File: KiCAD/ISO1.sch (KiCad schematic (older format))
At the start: 5 parts, among them J39 Conn_02x04_Odd_Even, J40 Conn_02x04_Odd_Even, U14 ISO7341c

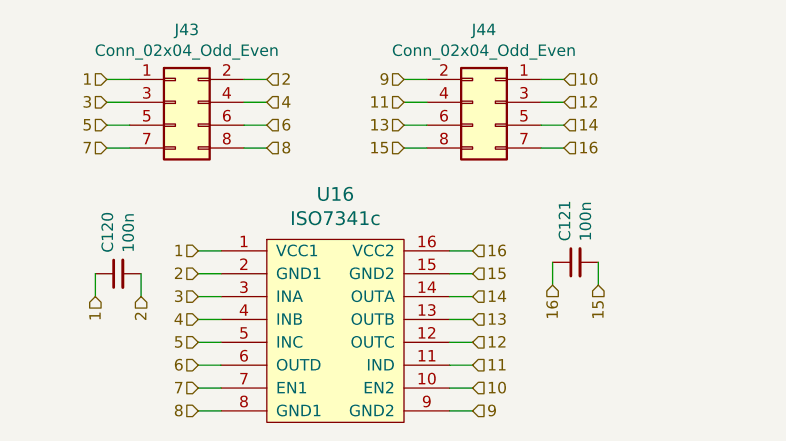
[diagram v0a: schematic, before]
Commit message: added usb, crystals
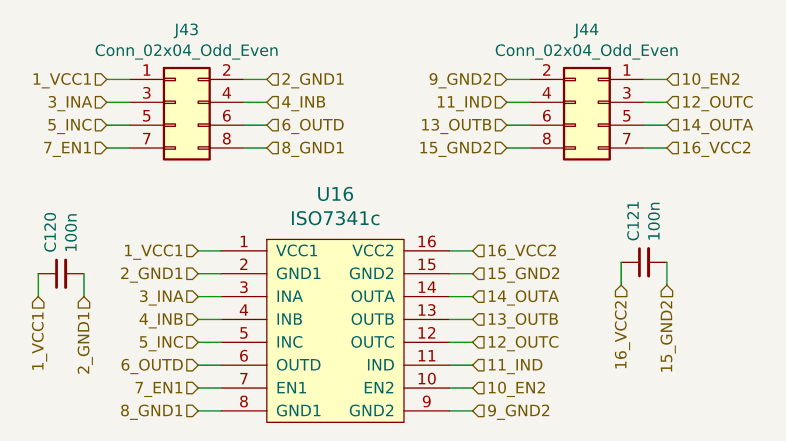
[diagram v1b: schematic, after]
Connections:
- net 1 renamed 1_VCC1
- net 10 renamed 10_EN2
- net 11 renamed 11_IND
- net 12 renamed 12_OUTC
- net 13 renamed 13_OUTB
- net 14 renamed 14_OUTA
- net 15 renamed 15_GND2
- net 16 renamed 16_VCC2
- net 2 renamed 2_GND1
- net 3 renamed 3_INA
- net 4 renamed 4_INB
- net 5 renamed 5_INC
- net 6 renamed 6_OUTD
- net 7 renamed 7_EN1
- net 8 renamed 8_GND1
- net 9 renamed 9_GND2
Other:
- moved on the sheet: C120, C121, J44
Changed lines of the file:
@@
 $Descr A4 11693 8268
 encoding utf-8
-Sheet 15 17
+Sheet 15 18
 Title ""
 Date ""
@@
 	1    0    0    -1
 $EndComp
-Text HLabel 2350 2800 3    50   Input ~ 0
-1
-Text HLabel 2550 2800 3    50   Input ~ 0
-2
+Text HLabel 2100 2800 3    50   Input ~ 0
+1_VCC1
+Text HLabel 2300 2800 3    50   Input ~ 0
+2_GND1
 $Comp
 L Device:C_Small C?
 U 1 1 5CDC49E7
-P 2450 2700
+P 2200 2700
 AR Path="/5CDBF57D/5CDC49E7" Ref="C?"  Part="1"
 AR Path="/5CE92451/5CDC49E7" Ref="C?"  Part="1"
@@
 AR Path="/5CDD240A/5CDC49E7" Ref="C118"  Part="1"
 AR Path="/5CDD240D/5CDC49E7" Ref="C120"  Part="1"
-F 0 "C120" H 2542 2746 50  0000 L CNN
-F 1 "100n" H 2542 2655 50  0000 L CNN
-F 2 "Capacitor_SMD:C_0402_1005Metric" H 2450 2700 50  0001 C CNN
-F 3 "~" H 2450 2700 50  0001 C CNN
-	1    2450 2700
+F 0 "C120" H 2292 2746 50  0000 L CNN
+F 1 "100n" H 2292 2655 50  0000 L CNN
+F 2 "Capacitor_SMD:C_0402_1005Metric" H 2200 2700 50  0001 C CNN
+F 3 "~" H 2200 2700 50  0001 C CNN
+	1    2200 2700
 	0    -1   -1   0
 $EndComp
 Wire Wire Line
-	2350 2800 2350 2700
-Wire Wire Line
-	2550 2800 2550 2700
+	2100 2800 2100 2700
+Wire Wire Line
+	2300 2800 2300 2700
 Text HLabel 2800 2600 0    50   Input ~ 0
-1
+1_VCC1
 Wire Wire Line
 	2800 2600 2900 2600
 Text HLabel 2800 2700 0    50   Input ~ 0
-2
+2_GND1
 Wire Wire Line
 	2800 2700 2900 2700
 Text HLabel 2800 2800 0    50   Input ~ 0
-3
+3_INA
 Wire Wire Line
 	2800 2800 2900 2800
 Text HLabel 2800 2900 0    50   Input ~ 0
-4
+4_INB
 Wire Wire Line
 	2800 2900 2900 2900
 Text HLabel 2800 3100 0    50   Input ~ 0
-6
+6_OUTD
 Wire Wire Line
 	2800 3100 2900 3100
 Text HLabel 2800 3300 0    50   Input ~ 0
-8
+8_GND1
 Wire Wire Line
 	2800 3300 2900 3300
@@
 	2800 3000 2900 3000
 Text HLabel 2800 3000 0    50   Input ~ 0
-5
+5_INC
 Text HLabel 2800 3200 0    50   Input ~ 0
-7
+7_EN1
 Text HLabel 4000 2600 2    50   Input ~ 0
-16
+16_VCC2
 Wire Wire Line
 	4000 2600 3900 2600
 Text HLabel 4000 2700 2    50   Input ~ 0
-15
+15_GND2
 Wire Wire Line
 	4000 2700 3900 2700
 Text HLabel 4000 2800 2    50   Input ~ 0
-14
+14_OUTA
 Wire Wire Line
 	4000 2800 3900 2800
 Text HLabel 4000 2900 2    50   Input ~ 0
-13
+13_OUTB
 Wire Wire Line
 	4000 2900 3900 2900
 Text HLabel 4000 3100 2    50   Input ~ 0
-11
+11_IND
 Wire Wire Line
 	4000 3100 3900 3100
 Text HLabel 4000 3300 2    50   Input ~ 0
-9
+9_GND2
 Wire Wire Line
 	4000 3300 3900 3300
@@
 	4000 3000 3900 3000
 Text HLabel 4000 3000 2    50   Input ~ 0
-12
+12_OUTC
 Text HLabel 4000 3200 2    50   Input ~ 0
-10
+10_EN2
 $Comp
 L Connector_Generic:Conn_02x04_Odd_Even J39
@@
 $EndComp
 Text HLabel 2400 1850 0    50   Input ~ 0
-1
+1_VCC1
 Wire Wire Line
 	2400 1850 2500 1850
 Text HLabel 2400 1950 0    50   Input ~ 0
-3
+3_INA
 Wire Wire Line
 	2400 1950 2500 1950
@@
 	2400 2050 2500 2050
 Text HLabel 2400 2050 0    50   Input ~ 0
-5
+5_INC
 Text HLabel 2400 2150 0    50   Input ~ 0
-7
+7_EN1
 Text HLabel 3100 1850 2    50   Input ~ 0
-2
+2_GND1
 Wire Wire Line
 	3100 1850 3000 1850
 Text HLabel 3100 1950 2    50   Input ~ 0
-4
+4_INB
 Wire Wire Line
 	3100 1950 3000 1950
 Text HLabel 3100 2050 2    50   Input ~ 0
-6
+6_OUTD
 Wire Wire Line
 	3100 2050 3000 2050
 Text HLabel 3100 2150 2    50   Input ~ 0
-8
+8_GND1
 Wire Wire Line
 	3100 2150 3000 2150
@@
 L Connector_Generic:Conn_02x04_Odd_Even J40
 U 1 1 5CDCDF09
-P 4100 1950
+P 4550 1950
 AR Path="/5CE35379/5CDCDF09" Ref="J40"  Part="1"
 AR Path="/5CDD240A/5CDCDF09" Ref="J42"  Part="1"
 AR Path="/5CDD240D/5CDCDF09" Ref="J44"  Part="1"
-F 0 "J44" H 4150 2267 50  0000 C CNN
-F 1 "Conn_02x04_Odd_Even" H 4150 2176 50  0000 C CNN
-F 2 "Connector_PinHeader_2.54mm:PinHeader_2x04_P2.54mm_Vertical" H 4100 1950 50  0001 C CNN
-F 3 "~" H 4100 1950 50  0001 C CNN
-	1    4100 1950
+F 0 "J44" H 4600 2267 50  0000 C CNN
+F 1 "Conn_02x04_Odd_Even" H 4600 2176 50  0000 C CNN
+F 2 "Connector_PinHeader_2.54mm:PinHeader_2x04_P2.54mm_Vertical" H 4550 1950 50  0001 C CNN
+F 3 "~" H 4550 1950 50  0001 C CNN
+	1    4550 1950
 	-1   0    0    -1
 $EndComp
-Text HLabel 3700 1850 0    50   Input ~ 0
-9
-Wire Wire Line
-	3700 1850 3800 1850
-Text HLabel 3700 1950 0    50   Input ~ 0
-11
-Wire Wire Line
-	3700 1950 3800 1950
-Wire Wire Line
-	3700 2150 3800 2150
-Wire Wire Line
-	3700 2050 3800 2050
-Text HLabel 3700 2050 0    50   Input ~ 0
-13
-Text HLabel 3700 2150 0    50   Input ~ 0
-15
-Text HLabel 4400 1850 2    50   Input ~ 0
-10
-Wire Wire Line
-	4400 1850 4300 1850
-Text HLabel 4400 1950 2    50   Input ~ 0
-12
-Wire Wire Line
-	4400 1950 4300 1950
-Text HLabel 4400 2050 2    50   Input ~ 0
-14
-Wire Wire Line
-	4400 2050 4300 2050
-Text HLabel 4400 2150 2    50   Input ~ 0
-16
-Wire Wire Line
-	4400 2150 4300 2150
-Text HLabel 4350 2750 3    50   Input ~ 0
-16
-Text HLabel 4550 2750 3    50   Input ~ 0
-15
+Text HLabel 4150 1850 0    50   Input ~ 0
+9_GND2
+Wire Wire Line
+	4150 1850 4250 1850
+Text HLabel 4150 1950 0    50   Input ~ 0
+11_IND
+Wire Wire Line
+	4150 1950 4250 1950
+Wire Wire Line
+	4150 2150 4250 2150
+Wire Wire Line
+	4150 2050 4250 2050
+Text HLabel 4150 2050 0    50   Input ~ 0
+13_OUTB
+Text HLabel 4150 2150 0    50   Input ~ 0
+15_GND2
+Text HLabel 4850 1850 2    50   Input ~ 0
+10_EN2
+Wire Wire Line
+	4850 1850 4750 1850
+Text HLabel 4850 1950 2    50   Input ~ 0
+12_OUTC
+Wire Wire Line
+	4850 1950 4750 1950
+Text HLabel 4850 2050 2    50   Input ~ 0
+14_OUTA
+Wire Wire Line
+	4850 2050 4750 2050
+Text HLabel 4850 2150 2    50   Input ~ 0
+16_VCC2
+Wire Wire Line
+	4850 2150 4750 2150
+Text HLabel 4650 2750 3    50   Input ~ 0
+16_VCC2
+Text HLabel 4850 2750 3    50   Input ~ 0
+15_GND2
 $Comp
 L Device:C_Small C?
 U 1 1 5CDD0F5D
-P 4450 2650
+P 4750 2650
 AR Path="/5CDBF57D/5CDD0F5D" Ref="C?"  Part="1"
 AR Path="/5CE92451/5CDD0F5D" Ref="C?"  Part="1"
@@
 AR Path="/5CDD240A/5CDD0F5D" Ref="C119"  Part="1"
 AR Path="/5CDD240D/5CDD0F5D" Ref="C121"  Part="1"
-F 0 "C121" H 4542 2696 50  0000 L CNN
-F 1 "100n" H 4542 2605 50  0000 L CNN
-F 2 "Capacitor_SMD:C_0402_1005Metric" H 4450 2650 50  0001 C CNN
-F 3 "~" H 4450 2650 50  0001 C CNN
-	1    4450 2650
+F 0 "C121" H 4842 2696 50  0000 L CNN
+F 1 "100n" H 4842 2605 50  0000 L CNN
+F 2 "Capacitor_SMD:C_0402_1005Metric" H 4750 2650 50  0001 C CNN
+F 3 "~" H 4750 2650 50  0001 C CNN
+	1    4750 2650
 	0    -1   -1   0
 $EndComp
 Wire Wire Line
-	4350 2750 4350 2650
-Wire Wire Line
-	4550 2750 4550 2650
+	4650 2750 4650 2650
+Wire Wire Line
+	4850 2750 4850 2650
 $EndSCHEMATC
